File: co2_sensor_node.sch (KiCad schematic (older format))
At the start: 6 parts

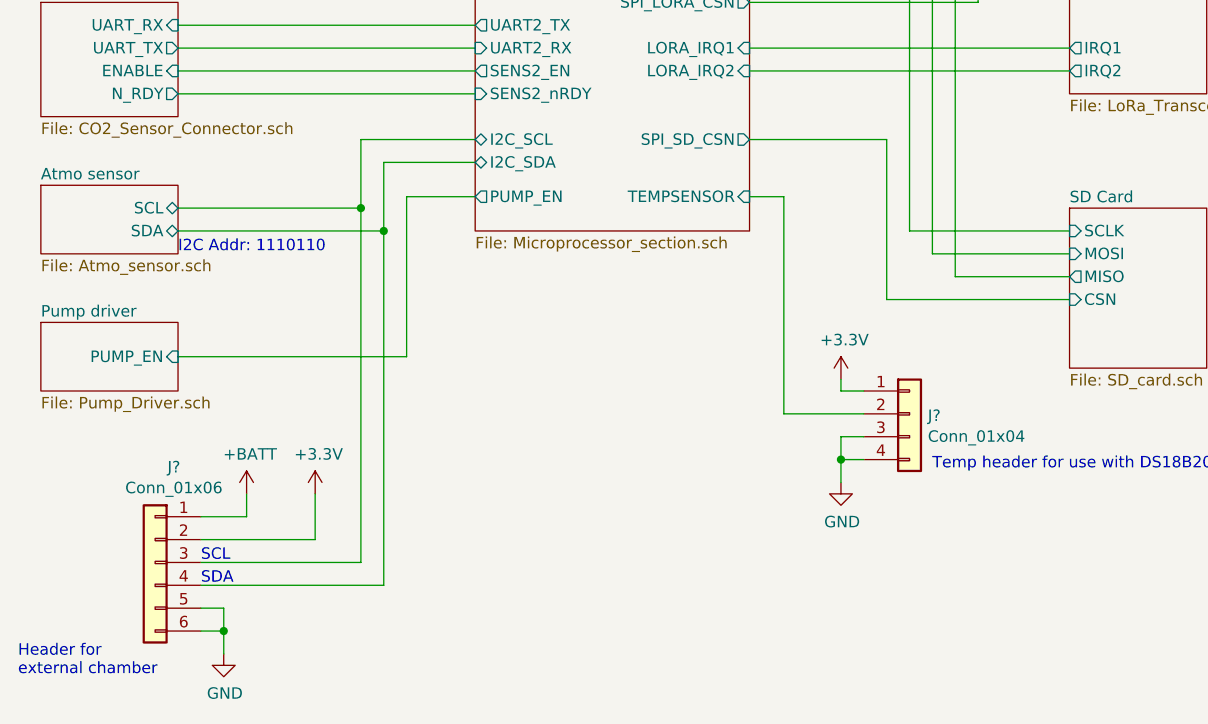
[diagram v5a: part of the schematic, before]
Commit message: Finish routing of Rev 1
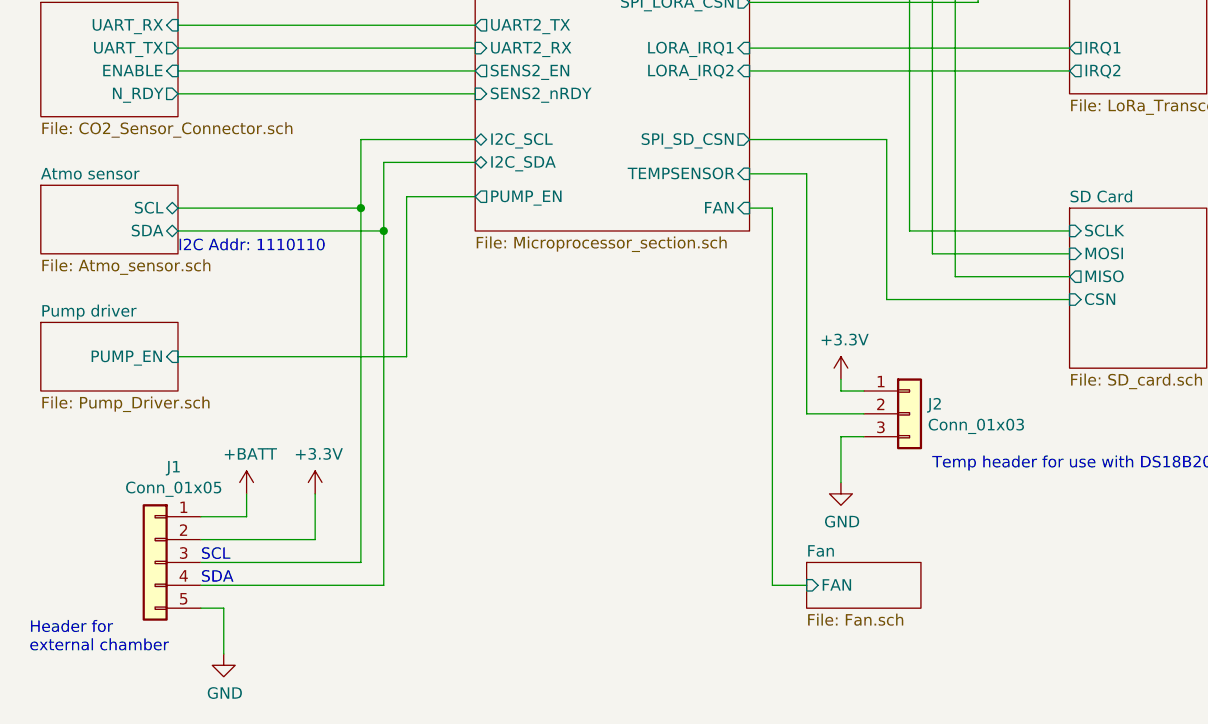
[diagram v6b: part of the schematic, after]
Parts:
- removed J?: Conn_01x04, Connector_JST:JST_XH_S4B-XH-A_1x04_P2.50mm_Horizontal, symbol Connector_Generic:Conn_01x04
- removed J?: Conn_01x06, Connector_JST:JST_XH_S6B-XH-A_1x06_P2.50mm_Horizontal, symbol Connector_Generic:Conn_01x06
- added J1: Conn_01x05, Connector_JST:JST_XH_B5B-XH-AM_1x05_P2.50mm_Vertical, symbol Connector_Generic:Conn_01x05
- added J2: Conn_01x03, Connector_JST:JST_XH_B3B-XH-AM_1x03_P2.50mm_Vertical, symbol Connector_Generic:Conn_01x03
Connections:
- net +3V3: now also J1.2 (Pin_2), J2.1 (Pin_1)
- net +BATT: now also J1.1 (Pin_1)
- net Atmo sensor/SCL: now also J1.3 (Pin_3)
- net Atmo sensor/SDA: now also J1.4 (Pin_4)
- net GND: now also J1.5 (Pin_5), J2.3 (Pin_3)
- net Microprocessor section/TEMPSENSOR: now also J2.2 (Pin_2)
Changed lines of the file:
@@
 $Descr A4 11693 8268
 encoding utf-8
-Sheet 1 9
+Sheet 1 10
 Title ""
 Date ""
@@
 F18 "LORA_IRQ2" I R 6100 3800 50
 F19 "PUMP_EN" O L 4900 4350 50
-F20 "TEMPSENSOR" I R 6100 4350 50
+F20 "TEMPSENSOR" I R 6100 4250 50
+F21 "FAN" I R 6100 4400 50
 $EndSheet
 Wire Wire Line
@@
 	3700 6150 3800 6150
 Wire Wire Line
-	3800 6150 3800 6250
-Wire Wire Line
 	3700 5750 3900 5750
 Wire Wire Line
@@
 Wire Wire Line
 	6500 5400 6600 5400
-Wire Wire Line
-	6100 4350 6250 4350
-Wire Wire Line
-	6250 4350 6250 5300
-Wire Wire Line
-	6250 5300 6600 5300
-$Comp
-L Connector_Generic:Conn_01x04 J?
-U 1 1 60D49B52
-P 6800 5300
-F 0 "J?" H 6880 5292 50  0000 L CNN
-F 1 "Conn_01x04" H 6880 5201 50  0000 L CNN
-F 2 "Connector_JST:JST_XH_S4B-XH-A_1x04_P2.50mm_Horizontal" H 6800 5300 50  0001 C CNN
-F 3 "~" H 6800 5300 50  0001 C CNN
-	1    6800 5300
-	1    0    0    -1
-$EndComp
-Wire Wire Line
-	6500 5600 6500 5500
-Wire Wire Line
-	6500 5500 6600 5500
-Wire Wire Line
-	6500 5400 6500 5500
-Connection ~ 6500 5500
 Text Notes 6900 5550 0    50   ~ 0
 Temp header for use with DS18B20 sensor\n
-Text Notes 2900 6450 0    50   ~ 0
-Header for\nexternal chamber
-$Comp
-L Connector_Generic:Conn_01x06 J?
-U 1 1 60D59C46
+Wire Wire Line
+	6350 4250 6350 5300
+Wire Wire Line
+	6100 4250 6350 4250
+Wire Wire Line
+	6350 5300 6600 5300
+$Sheet
+S 6350 5950 500  200
+U 60D4D720
+F0 "Fan" 50
+F1 "Fan.sch" 50
+F2 "FAN" I L 6350 6050 50
+$EndSheet
+Wire Wire Line
+	6350 6050 6200 6050
+Wire Wire Line
+	6200 6050 6200 4400
+Wire Wire Line
+	6200 4400 6100 4400
+$Comp
+L Connector_Generic:Conn_01x05 J?
+U 1 1 60D57F3B
 P 3500 5950
-F 0 "J?" H 3418 6367 50  0000 C CNN
-F 1 "Conn_01x06" H 3418 6276 50  0000 C CNN
-F 2 "Connector_JST:JST_XH_S6B-XH-A_1x06_P2.50mm_Horizontal" H 3500 5950 50  0001 C CNN
+AR Path="/60A49A7C/60D57F3B" Ref="J?"  Part="1"
+AR Path="/60A4AC4A/60D57F3B" Ref="J?"  Part="1"
+AR Path="/60D57F3B" Ref="J1"  Part="1"
+F 0 "J1" H 3418 6367 50  0000 C CNN
+F 1 "Conn_01x05" H 3418 6276 50  0000 C CNN
+F 2 "Connector_JST:JST_XH_B5B-XH-AM_1x05_P2.50mm_Vertical" H 3500 5950 50  0001 C CNN
 F 3 "~" H 3500 5950 50  0001 C CNN
 	1    3500 5950
 	-1   0    0    -1
 $EndComp
-Wire Wire Line
-	3700 6250 3800 6250
-Wire Wire Line
-	3800 6250 3800 6350
-Connection ~ 3800 6250
+Text Notes 2950 6350 0    50   ~ 0
+Header for\nexternal chamber
+Wire Wire Line
+	3800 6150 3800 6350
+$Comp
+L Connector_Generic:Conn_01x03 J2
+U 1 1 60D61D13
+P 6800 5300
+F 0 "J2" H 6880 5342 50  0000 L CNN
+F 1 "Conn_01x03" H 6880 5251 50  0000 L CNN
+F 2 "Connector_JST:JST_XH_B3B-XH-AM_1x03_P2.50mm_Vertical" H 6800 5300 50  0001 C CNN
+F 3 "~" H 6800 5300 50  0001 C CNN
+	1    6800 5300
+	1    0    0    -1
+$EndComp
+Wire Wire Line
+	6500 5400 6500 5600
 $EndSCHEMATC
